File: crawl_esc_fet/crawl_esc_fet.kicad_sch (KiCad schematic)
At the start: 27 parts, among them Q1 (DNP)TPHR8504PL,L1Q, Q11 (DNP)TPHR8504PL,L1Q, Q3 (DNP)TPHR8504PL,L1Q, Q5 (DNP)TPHR8504PL,L1Q, Q7 (DNP)TPHR8504PL,L1Q, Q9 (DNP)TPHR8504PL,L1Q

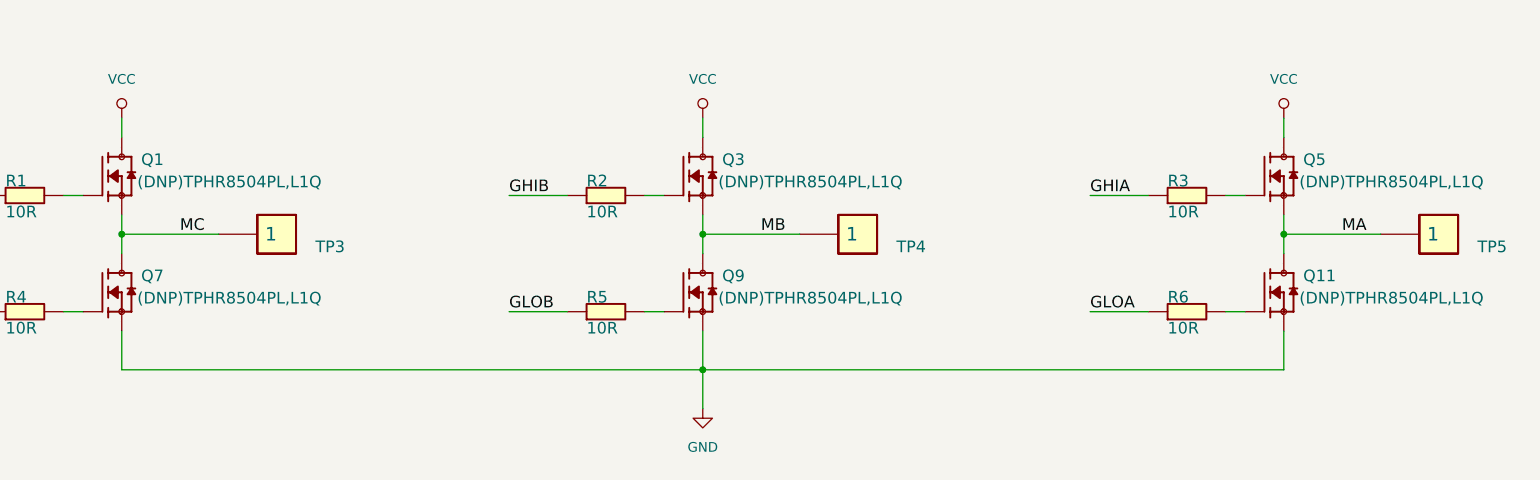
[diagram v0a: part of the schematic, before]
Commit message: change stepup isens layout
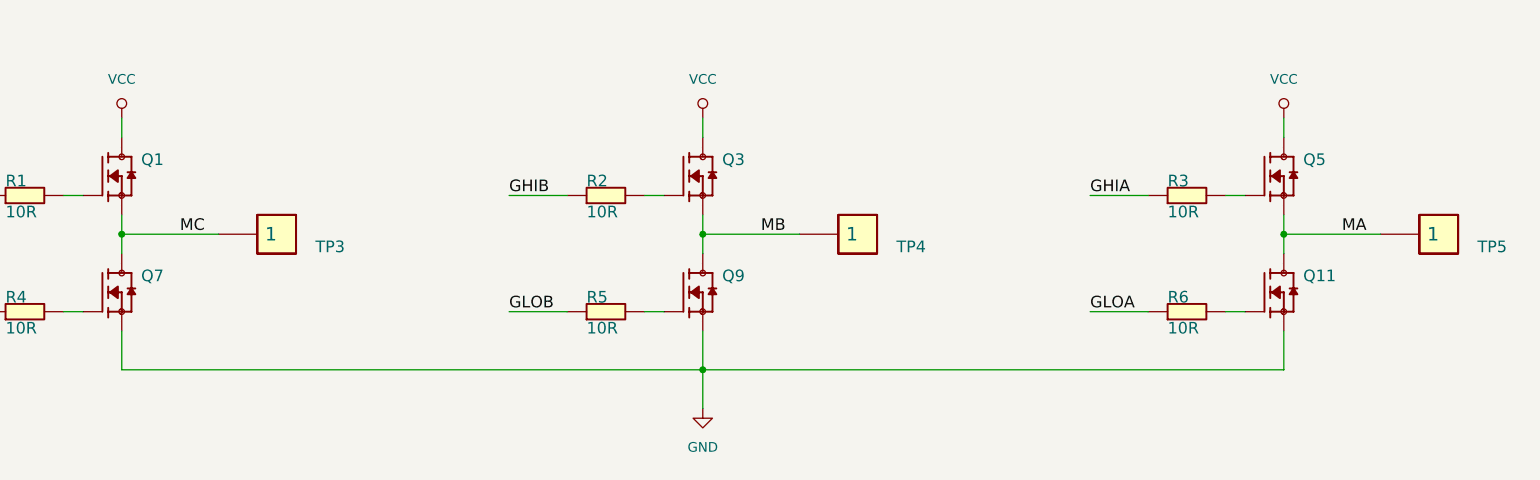
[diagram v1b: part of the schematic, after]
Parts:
- Q1, Q11, Q3, Q5, Q7, Q9: value (DNP)TPHR8504PL,L1Q -> (none)
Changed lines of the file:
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@@
       (effects (font (size 1.524 1.524)) (justify left bottom))
     )
-    (property "Value" "(DNP)TPHR8504PL,L1Q" (id 1) (at 281.432 128.651 0)
+    (property "Value" "" (id 1) (at 281.432 128.651 0)
       (effects (font (size 1.524 1.524)) (justify left bottom))
     )
@@
       (effects (font (size 1.524 1.524)) (justify left bottom))
     )
-    (property "Value" "(DNP)TPHR8504PL,L1Q" (id 1) (at 281.432 113.411 0)
+    (property "Value" "" (id 1) (at 281.432 113.411 0)
       (effects (font (size 1.524 1.524)) (justify left bottom))
     )
@@
       (effects (font (size 1.524 1.524)) (justify left bottom))
     )
-    (property "Value" "(DNP)TPHR8504PL,L1Q" (id 1) (at 205.232 128.651 0)
+    (property "Value" "" (id 1) (at 205.232 128.651 0)
       (effects (font (size 1.524 1.524)) (justify left bottom))
     )
@@
       (effects (font (size 1.524 1.524)) (justify left bottom))
     )
-    (property "Value" "(DNP)TPHR8504PL,L1Q" (id 1) (at 205.232 113.411 0)
+    (property "Value" "" (id 1) (at 205.232 113.411 0)
       (effects (font (size 1.524 1.524)) (justify left bottom))
     )
@@
       (effects (font (size 1.524 1.524)) (justify left bottom))
     )
-    (property "Value" "(DNP)TPHR8504PL,L1Q" (id 1) (at 129.032 128.651 0)
+    (property "Value" "" (id 1) (at 129.032 128.651 0)
       (effects (font (size 1.524 1.524)) (justify left bottom))
     )
@@
       (effects (font (size 1.524 1.524)) (justify left bottom))
     )
-    (property "Value" "(DNP)TPHR8504PL,L1Q" (id 1) (at 129.032 113.411 0)
+    (property "Value" "" (id 1) (at 129.032 113.411 0)
       (effects (font (size 1.524 1.524)) (justify left bottom))
     )
@@
     )
     (path "/00000000-0000-0000-0000-0000623ffc38"
-      (reference "Q1") (unit 1) (value "(DNP)TPHR8504PL,L1Q") (footprint "")
+      (reference "Q1") (unit 1) (value "TPHR8504PL,L1Q") (footprint "")
     )
     (path "/00000000-0000-0000-0000-0000623ffc22"
-      (reference "Q3") (unit 1) (value "(DNP)TPHR8504PL,L1Q") (footprint "")
+      (reference "Q3") (unit 1) (value "TPHR8504PL,L1Q") (footprint "")
     )
     (path "/00000000-0000-0000-0000-0000623ffc1c"
-      (reference "Q5") (unit 1) (value "(DNP)TPHR8504PL,L1Q") (footprint "")
+      (reference "Q5") (unit 1) (value "TPHR8504PL,L1Q") (footprint "")
     )
     (path "/00000000-0000-0000-0000-0000623ffc2d"
-      (reference "Q7") (unit 1) (value "(DNP)TPHR8504PL,L1Q") (footprint "")
+      (reference "Q7") (unit 1) (value "TPHR8504PL,L1Q") (footprint "")
     )
     (path "/00000000-0000-0000-0000-0000623ffc1d"
-      (reference "Q9") (unit 1) (value "(DNP)TPHR8504PL,L1Q") (footprint "")
+      (reference "Q9") (unit 1) (value "TPHR8504PL,L1Q") (footprint "")
     )
     (path "/00000000-0000-0000-0000-0000623ffc1b"
-      (reference "Q11") (unit 1) (value "(DNP)TPHR8504PL,L1Q") (footprint "")
+      (reference "Q11") (unit 1) (value "TPHR8504PL,L1Q") (footprint "")
     )
     (path "/00000000-0000-0000-0000-0000623ffc1a"
